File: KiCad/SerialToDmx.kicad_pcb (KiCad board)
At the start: 4 copper layers, 158 x 54 mm, 39 parts, among them J1 NAC3MPXXA, J10 Conn_01x08_Pin, J11 Conn_01x08_Pin, J2 NAC3MPXXB, J3 NC3FAV, J4 NC3MAV, J5 NC4FAV, J6 Conn_01x08_Socket, J7 Conn_01x08_Socket, J8 Conn_01x08_Pin, J9 Conn_01x08_Pin, U1 XIAO ESP32 C3, U2 ISOM8710DFFR, U3 ISOM8710DFFR, U4 ISOM8710DFFR, U5 THVD1512DGS, U6 SN74LV1T34DBV

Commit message: With Files
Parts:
- removed the H6 at (206.5, 106.8)
- added F11: 01110501Z, Custom_Littlefuse:fuseholder_111_501_Part1, F.Cu at (153.2, 59.5)
- added F12: 01110501Z, Custom_Littlefuse:fuseholder_111_501_Part2, F.Cu at (134.4, 59.5)
- added H10: MountingHole, MountingHole:MountingHole_3.2mm_M3, F.Cu at (203.0, 111.0)
- added H19: MountingHole, Panelization:mouse-bite-2mm-slot, F.Cu at (209.0, 71.0)
- added H20: MountingHole, Panelization:mouse-bite-2mm-slot, F.Cu at (209.0, 77.0)
- added H21: MountingHole, Panelization:mouse-bite-2mm-slot, F.Cu at (179.0, 71.0)
- added H22: MountingHole, Panelization:mouse-bite-2mm-slot, F.Cu at (179.0, 77.0)
- added H4: MountingHole_Pad, MountingHole:MountingHole_3.2mm_M3_DIN965_Pad, F.Cu at (161.9, 58.1)
- added H5: MountingHole, MountingHole:MountingHole_3.2mm_M3, F.Cu at (173.0, 58.5)
- added H8: MountingHole, MountingHole:MountingHole_3.2mm_M3, F.Cu at (209.0, 89.5)
- added H9: MountingHole, MountingHole:MountingHole_3.2mm_M3, F.Cu at (179.0, 111.0)
- added R5: 10kR, Resistor_SMD:R_0402_1005Metric, F.Cu at (77.0, 71.0)
- added TH1: Thermistor_PTC, Resistor_SMD:R_0402_1005Metric, F.Cu at (77.0, 70.0)
- added U7: NSM2012, Package_SO:SOIC-8_3.9x4.9mm_P1.27mm, F.Cu at (59.8, 84.8)
- added X1: 1217861-1, Custom_Connector_Faston:Faston_01x01_pin, F.Cu at (170.0, 101.5)
- added X11: 1217861-1, Custom_Connector_Faston:Faston_01x01_pin, F.Cu at (170.0, 120.5)
- added X12: 1217861-1, Custom_Connector_Faston:Faston_01x01_pin, F.Cu at (176.0, 120.5)
- added X13: 1217861-1, Custom_Connector_Faston:Faston_01x01_pin, F.Cu at (182.0, 120.5)
- added X14: 1217861-1, Custom_Connector_Faston:Faston_01x01_pin, F.Cu at (188.0, 120.5)
- added X15: 1217861-1, Custom_Connector_Faston:Faston_01x01_pin, F.Cu at (194.0, 120.5)
- added X16: 1217861-1, Custom_Connector_Faston:Faston_01x01_pin, F.Cu at (200.0, 120.5)
- added X17: 1217861-1, Custom_Connector_Faston:Faston_01x01_pin, F.Cu at (205.9, 120.5)
- added X18: 1217861-1, Custom_Connector_Faston:Faston_01x01_pin, F.Cu at (212.0, 120.5)
- added X2: 1217861-1, Custom_Connector_Faston:Faston_01x01_pin, F.Cu at (176.1, 101.5)
- added X3: 1217861-1, Custom_Connector_Faston:Faston_01x01_pin, F.Cu at (182.1, 101.5)
- added X4: 1217861-1, Custom_Connector_Faston:Faston_01x01_pin, F.Cu at (188.1, 101.5)
- added X5: 1217861-1, Custom_Connector_Faston:Faston_01x01_pin, F.Cu at (194.1, 101.5)
- added X6: 1217861-1, Custom_Connector_Faston:Faston_01x01_pin, F.Cu at (200.1, 101.5)
- added X61: 63994-1, Custom_Connector_Faston:Faston_01x01_socket, F.Cu at (87.5, 120.5)
- added X62: 63994-1, Custom_Connector_Faston:Faston_01x01_socket, F.Cu at (93.5, 120.5)
- added X63: 63994-1, Custom_Connector_Faston:Faston_01x01_socket, F.Cu at (99.5, 120.4)
- added X64: 63994-1, Custom_Connector_Faston:Faston_01x01_socket, F.Cu at (105.5, 120.4)
- added X65: 63994-1, Custom_Connector_Faston:Faston_01x01_socket, F.Cu at (111.5, 120.5)
- added X66: 63994-1, Custom_Connector_Faston:Faston_01x01_socket, F.Cu at (117.5, 120.4)
- added X67: 63994-1, Custom_Connector_Faston:Faston_01x01_socket, F.Cu at (123.5, 120.4)
- added X68: 63994-1, Custom_Connector_Faston:Faston_01x01_socket, F.Cu at (129.5, 120.4)
- added X7: 1217861-1, Custom_Connector_Faston:Faston_01x01_pin, F.Cu at (206.1, 101.5)
- added X71: 63994-1, Custom_Connector_Faston:Faston_01x01_socket, F.Cu at (87.5, 59.5)
- added X72: 63994-1, Custom_Connector_Faston:Faston_01x01_socket, F.Cu at (93.5, 59.5)
- added X73: 63994-1, Custom_Connector_Faston:Faston_01x01_socket, F.Cu at (99.5, 59.5)
- added X74: 63994-1, Custom_Connector_Faston:Faston_01x01_socket, F.Cu at (105.5, 59.5)
- added X75: 63994-1, Custom_Connector_Faston:Faston_01x01_socket, F.Cu at (111.5, 59.5)
- added X76: 63994-1, Custom_Connector_Faston:Faston_01x01_socket, F.Cu at (117.5, 59.5)
- added X77: 63994-1, Custom_Connector_Faston:Faston_01x01_socket, F.Cu at (123.5, 59.5)
- added X78: 63994-1, Custom_Connector_Faston:Faston_01x01_socket, F.Cu at (129.5, 59.5)
- added X8: 1217861-1, Custom_Connector_Faston:Faston_01x01_pin, F.Cu at (212.1, 101.5)
- added X81: 1217861-1, Custom_Connector_Faston:Faston_01x01_pin, F.Cu at (170.0, 65.5)
- added X82: 1217861-1, Custom_Connector_Faston:Faston_01x01_pin, F.Cu at (176.0, 65.5)
- added X83: 1217861-1, Custom_Connector_Faston:Faston_01x01_pin, F.Cu at (182.0, 65.5)
- added X84: 1217861-1, Custom_Connector_Faston:Faston_01x01_pin, F.Cu at (188.0, 65.5)
- added X85: 1217861-1, Custom_Connector_Faston:Faston_01x01_pin, F.Cu at (194.0, 65.5)
- added X86: 1217861-1, Custom_Connector_Faston:Faston_01x01_pin, F.Cu at (200.0, 65.5)
- added X87: 1217861-1, Custom_Connector_Faston:Faston_01x01_pin, F.Cu at (206.0, 65.5)
- added X88: 1217861-1, Custom_Connector_Faston:Faston_01x01_pin, F.Cu at (212.0, 65.5)
- added X91: 1217861-1, Custom_Connector_Faston:Faston_01x01_pin, F.Cu at (170.1, 82.5)
- added X92: 1217861-1, Custom_Connector_Faston:Faston_01x01_pin, F.Cu at (176.1, 82.5)
- added X93: 1217861-1, Custom_Connector_Faston:Faston_01x01_pin, F.Cu at (182.1, 82.5)
- added X94: 1217861-1, Custom_Connector_Faston:Faston_01x01_pin, F.Cu at (188.1, 82.5)
- added X95: 1217861-1, Custom_Connector_Faston:Faston_01x01_pin, F.Cu at (194.1, 82.5)
- added X96: 1217861-1, Custom_Connector_Faston:Faston_01x01_pin, F.Cu at (200.1, 82.5)
- added X97: 1217861-1, Custom_Connector_Faston:Faston_01x01_pin, F.Cu at (206.1, 82.5)
- added X98: 1217861-1, Custom_Connector_Faston:Faston_01x01_pin, F.Cu at (212.1, 82.5)
- C1: value 0.1uC -> 100nF; footprint Capacitor_SMD:C_0402_1005Metric -> Capacitor_SMD:C_0402_1005Metric_Pad0.74x0.62mm_HandSolder
- D1: value 1N4005 -> D; footprint Diode_SMD:D_0402_1005Metric -> Resistor_SMD:R_0402_1005Metric
- H1: value MountingHole -> MountingHole_Pad; footprint MountingHole:MountingHole_3.2mm_M3 -> MountingHole:MountingHole_3.2mm_M3_DIN965_Pad
- H11: renamed from H7; value Mousebite -> MountingHole
- H12: renamed from H8; value Mousebite -> MountingHole
- H13: renamed from H9; value Mousebite -> MountingHole
- H14: renamed from H10; value Mousebite -> MountingHole
- H15: renamed from H11; value Mousebite -> MountingHole
- H16: renamed from H12; value Mousebite -> MountingHole; footprint Panelization:mouse-bite-3.5mm-slot -> Panelization:mouse-bite-2mm-slot
- H17: renamed from H13; value Mousebite -> MountingHole; footprint Panelization:mouse-bite-3.5mm-slot -> Panelization:mouse-bite-2mm-slot
- H18: renamed from H14; value Mousebite -> MountingHole
- H2: renamed from H3; value MountingHole -> MountingHole_Pad; footprint MountingHole:MountingHole_3.2mm_M3 -> MountingHole:MountingHole_3.2mm_M3_DIN965_Pad
- H3: renamed from H5; value MountingHole -> MountingHole_Pad; footprint MountingHole:MountingHole_3.2mm_M3 -> MountingHole:MountingHole_3.2mm_M3_DIN965_Pad
- J1: footprint NeutrikCustom:NAC3MPXXA -> Custom_Neutrik:NAC3MPXXA
- J10, J11, J8, J9: value Conn_01x08_Pin -> ~; footprint Connector_Faston_Custom:Faston_01x08_pin -> Custom_Connector_Faston:Faston_01x08_pin
- J2: footprint NeutrikCustom:NAC3MPXXB -> Custom_Neutrik:NAC3MPXXB
- J3: footprint NeutrikCustom:NC3FAV -> Connector_Audio:Jack_XLR_Neutrik_NC3FAV_Vertical
- J4: footprint NeutrikCustom:NC3MAV -> Connector_Audio:Jack_XLR_Neutrik_NC3MAV_Vertical
- J5: footprint NeutrikCustom:NC4FAV -> Connector_Audio:Jack_XLR_Neutrik_NC4FAV_Vertical
- J6, J7: value Conn_01x08_Socket -> ~; footprint Connector_Faston_Custom:Faston_01x08_socket -> Custom_Connector_Faston:Faston_01x08_socket
- PS1: footprint IRM-45-12:CONV_IRM-45-12 -> Custom_Meanwell:CONV_IRM-45-12
- PS2: footprint CONV_R-78E5.0-0.5:CONV_R-78E5.0-0.5 -> Custom_Recom:CONV_R-78E5.0-0.5
- PS3: footprint TracoCustom:CONV_TEA_1-0505 -> Converter_DCDC:Converter_DCDC_TRACO_TEA1-xxxx_THT
- U2: renamed from U5; footprint TICustom:DGS0010A_N -> Custom_TI:DGS0010A_N
- U3: renamed from U4; footprint TICustom:ISOM8710 -> Custom_TI:ISOM8710
- U4: renamed from U2; footprint TICustom:ISOM8710 -> Custom_TI:ISOM8710
- U5: renamed from U3; footprint TICustom:ISOM8710 -> Custom_TI:ISOM8710
- moved H1 185.3 mm to (58.1, 58.1)
- moved H2 153.9 mm to (58.1, 121.9)
- moved H3 76.1 mm to (161.9, 121.9)
- moved H17 70.9 mm to (173.0, 96.0)
- moved D1 65.8 mm to (65.5, 60.5), turned to 0 degrees
- moved U3 62.0 mm to (75.0, 121.0), turned to 180 degrees
- moved R3 61.8 mm to (69.5, 115.5), turned to 0 degrees
- moved J4 60.3 mm to (93.2, 90.0), turned to 0 degrees
- moved U2 58.0 mm to (82.0, 116.0), turned to 90 degrees
- moved R2 57.7 mm to (69.5, 114.0), turned to 0 degrees
- moved R1 57.4 mm to (80.5, 120.0), turned to 0 degrees
- moved U5 57.2 mm to (75.0, 117.0), turned to 0 degrees
- moved U1 54.6 mm to (72.5, 66.0), turned to 90 degrees
- moved U4 52.5 mm to (75.0, 113.0), turned to 0 degrees
- moved PS3 51.5 mm to (71.5, 110.0)
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- renumbered H2 to H6, H4 to H7, R3 to R1, R1 to R3
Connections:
- J5 pad 2: GND -> LED-GND
- PS1 pad AC/L: L -> L-Fused
- U1 pad 5: unconnected-(U1-D4-Pad5) -> LED-Current-Sensor
- U1 pad 6: unconnected-(U1-D5-Pad6) -> Temperature Sensor
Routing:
- net N: track 128.5 -> 17.7 mm
- net GND: track 113.6 -> 8.70 mm, vias 23 -> 50
- net L: track 122.2 -> 35.9 mm
- net GND_Iso: track 40.9 -> 110.9 mm, vias 1 -> 5
- net DMX_TX: track 17.7 -> 72.7 mm
- net DMX_RX: track 20.9 -> 74.4 mm, vias 1 -> 0
- net DMX_DRIVE: track 12.5 -> 60.1 mm
- net Net-(X13-Pad1): track 0.00 -> 42.5 mm
- net 3V3: track 43.9 -> 2.47 mm, vias 0 -> 2
- net DMX+: track 89.8 -> 129.5 mm, vias 0 -> 3
- net 12V: track 85.8 -> 48.2 mm
- net DMX-: track 84.2 -> 115.5 mm
- net Net-(X1-Pad1): track 0.00 -> 24.1 mm
- net Net-(X12-Pad1): track 0.00 -> 24.1 mm
- net Net-(J10-Pin_3): track 22.7 -> 0.00 mm
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- added copper zone on In2.Cu, net 3V3
- added copper zone on In1.Cu, net 5V
- added copper zone on F.Cu, net GND
- added copper zone on In1.Cu, net GND
- added copper zone on In2.Cu, net GND
- added copper zone on F.Cu, net GND-Connection-In-Termination
- added copper zone on In2.Cu, net GND_Iso
- added copper zone on In1.Cu, net L
- added copper zone on In2.Cu, net L
- added copper zone on F.Cu, net L-switched
- added copper zone on F.Cu, net LED-GND
- added copper zone on In2.Cu, net LED-GND
- added copper zone on F.Cu, net N
- added copper zone on In1.Cu, net N
- added copper zone on In1.Cu, net VCC_Iso
- removed copper zone on In2.Cu, net 5V
- removed copper zone on B.Cu, net GND-Connection-Out-Termination
- removed copper zone on In1.Cu, net GND-Connection-Out-Termination
- removed copper zone on In2.Cu, net GND-Connection-Out-Termination
- removed copper zone on B.Cu, net GND_Iso
- removed copper zone on In2.Cu, net N-switched
- removed copper zone on In2.Cu, net VCC_Iso
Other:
- board size 158 x 54 mm -> 160 x 70 mm

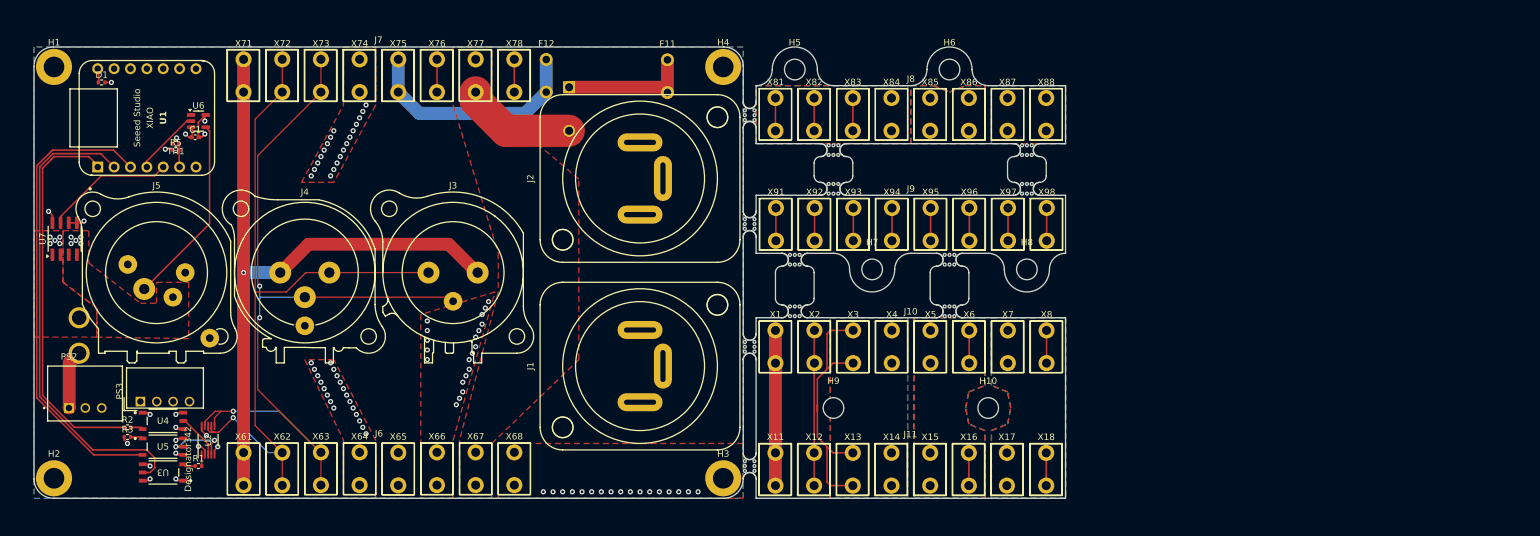
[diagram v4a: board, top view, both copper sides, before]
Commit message: Switched Female and Male XLR 3-Pin Connectors
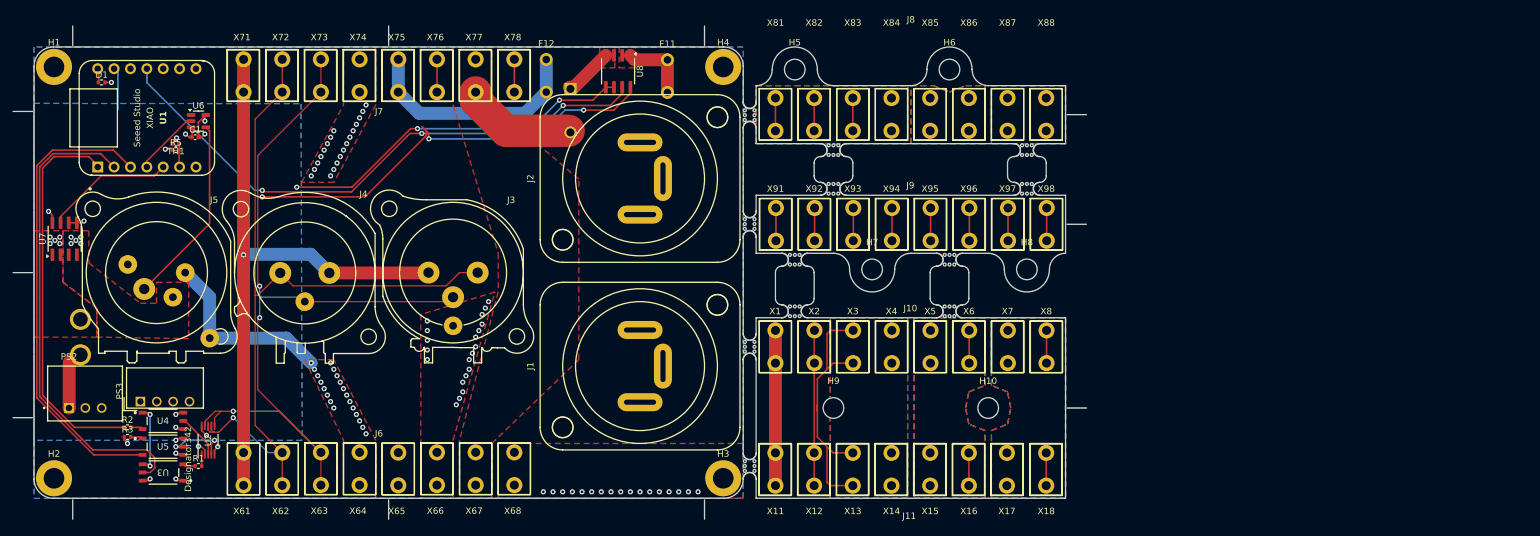
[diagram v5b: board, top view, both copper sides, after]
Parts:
- added U8: NSM2012-10B5R-DSPR, Package_SO:SOIC-8_3.9x4.9mm_P1.27mm, F.Cu at (145.6, 58.8)
- J3: value NC3FAV -> NC3MAV; footprint Connector_Audio:Jack_XLR_Neutrik_NC3FAV_Vertical -> Custom_Neutrik:NC3MAV
- J4: value NC3MAV -> NC3FAV; footprint Connector_Audio:Jack_XLR_Neutrik_NC3MAV_Vertical -> Custom_Neutrik:NC3FAV
- J5: footprint Connector_Audio:Jack_XLR_Neutrik_NC4FAV_Vertical -> Custom_Neutrik:NC4FAV
- TH1: value Thermistor_PTC -> TMP61-Q1
- U7: value NSM2012 -> NSM2012-10B5R-DSPR
- moved J5 4.45 mm to (74.0, 90.0)
- moved J3 3.81 mm to (120.0, 90.0)
- moved J4 3.81 mm to (97.0, 90.0)
- moved PS1 0.32 mm to (100.0, 82.5)
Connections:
- net GND-Connection-Bridge renamed PE-Connection-Bridge
- net GND-Connection-In-Termination renamed PE-Connection-In-Termination
- H1 pad 1: GND -> PE
- H2 pad 1: GND -> PE
- H3 pad 1: GND -> PE
- H4 pad 1: GND -> PE
- J1 pad G: GND -> PE
- J2 pad G: GND -> PE
- J5 pad 1: GND -> PE
- J5 pad G: GND -> PE
- PS1 pad AC/L: L-Fused -> L_Measured
- U1 pad 11: unconnected-(U1-D10-Pad11) -> AC-Current-Sensor
- X64 pad 1: GND -> PE
- X74 pad 1: GND -> PE
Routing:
- net AC-Current-Sensor: track 0.00 -> 90.2 mm, vias 0 -> 3
- net GND: track 8.70 -> 78.9 mm, vias 50 -> 13
- net 5V: track 10.4 -> 78.8 mm, vias 5 -> 8
- net PE: track 0.00 -> 29.1 mm, vias 0 -> 40
- net GND_Iso: track 110.9 -> 101.0 mm
- net L-Fused: track 20.6 -> 11.1 mm
- net DMX-: track 115.5 -> 125.0 mm
- net L_Measured: track 0.00 -> 7.74 mm
- net DMX+: track 129.5 -> 130.6 mm
- added copper zone on F.Cu, net L-Fused
- added copper zone on F.Cu, net L_Measured
- added copper zone on B.Cu, net PE
- added copper zone on F.Cu, net PE
- added copper zone on In1.Cu, net PE
- added copper zone on In2.Cu, net PE
- removed copper zone on In2.Cu, net GND
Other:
- board size 160 x 70 mm -> 166.5 x 76.5 mm
